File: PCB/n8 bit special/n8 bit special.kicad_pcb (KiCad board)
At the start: 2 copper layers, 99.7 x 97.8 mm, 36 parts, among them J1 PowerPort, J2 PORT0, J3 PORT2, J4 PORT1, J5 PORT3, J6 Conn_02x08_Odd_Even, SW1 SW_Push_Dual, U1 W65C02SxP, U2 CY62256-70PC, U3 CY62256-70PC, U4 28C256, U5 74LS21, U6 22V10C, U7 DS1813, X1 2Mhz

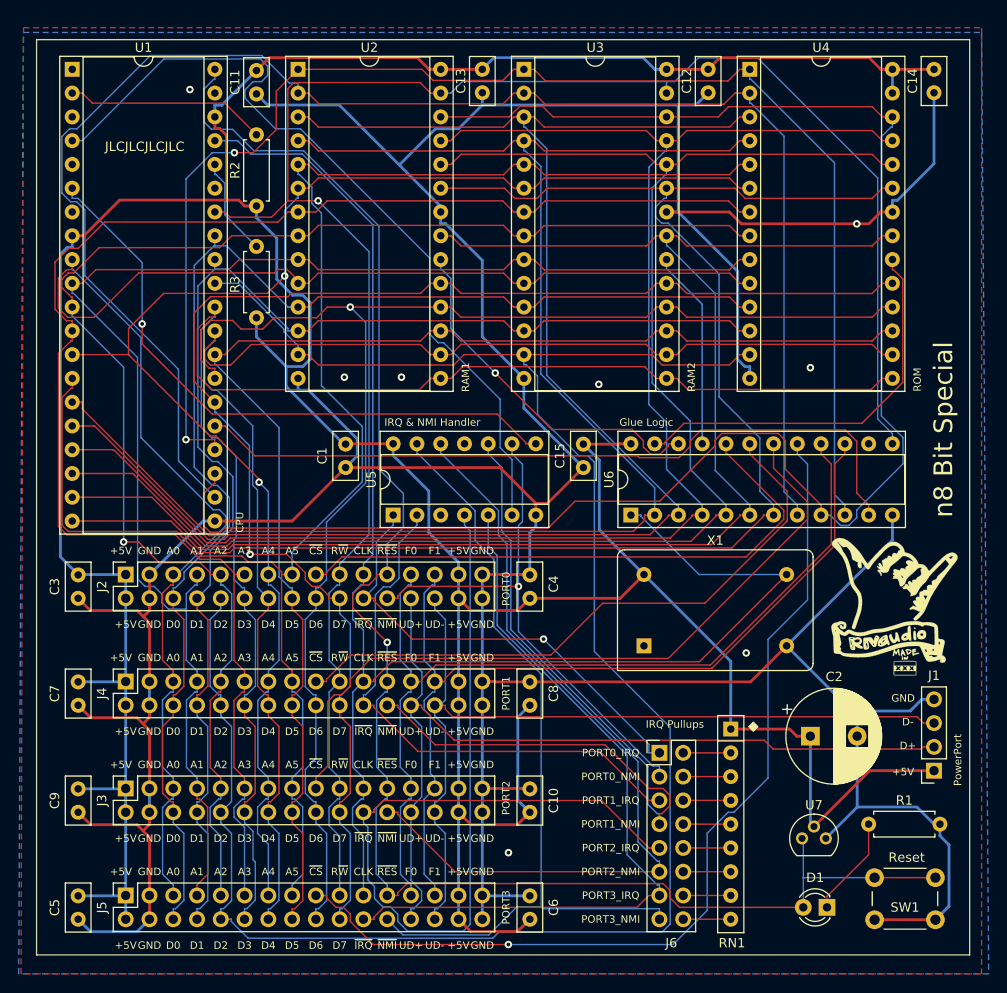
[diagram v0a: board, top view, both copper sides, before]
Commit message: New placement and parts for v2
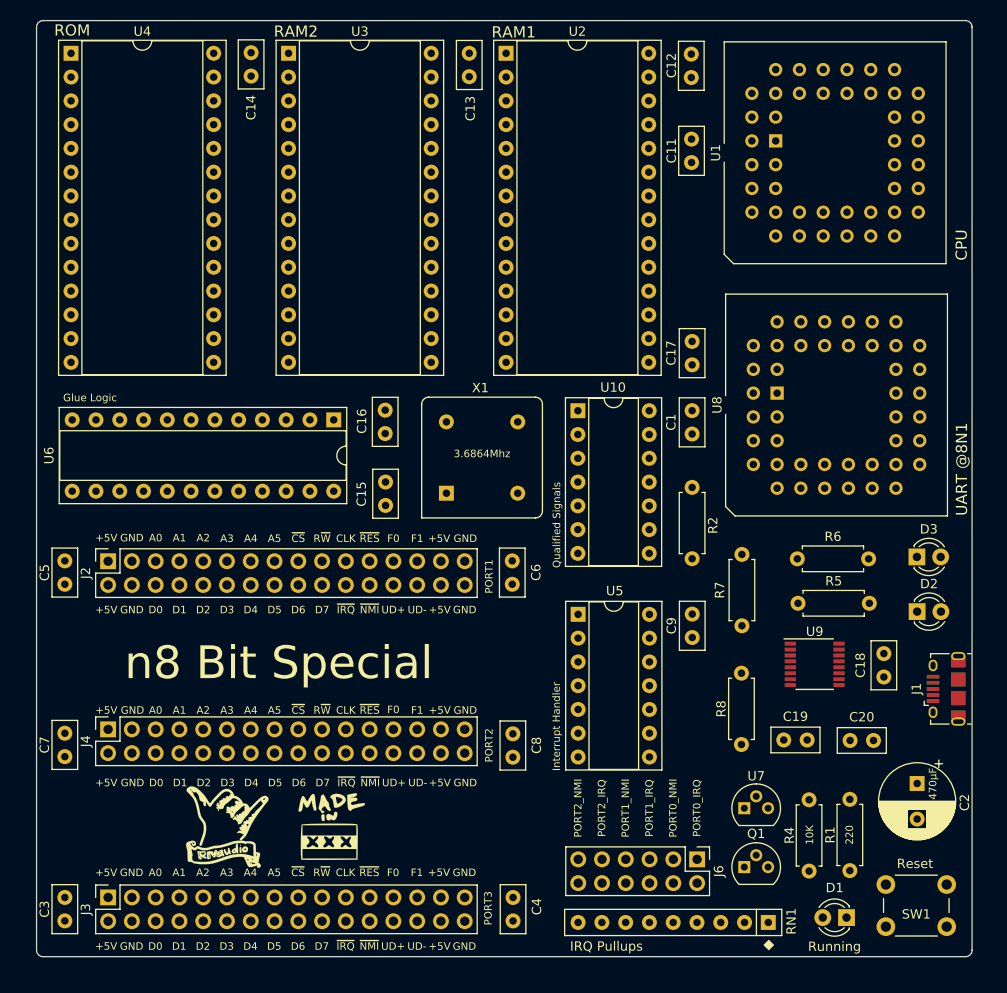
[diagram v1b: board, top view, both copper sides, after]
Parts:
- removed C10: 100nf, Capacitor_THT:C_Disc_D5.0mm_W2.5mm_P2.50mm
- removed J5: PORT3, Connector_PinSocket_2.54mm:PinSocket_2x16_P2.54mm_Vertical
- removed R3: 3K3, Resistor_THT:R_Axial_DIN0207_L6.3mm_D2.5mm_P7.62mm_Horizontal
- added C16: 100nf, Capacitor_THT:C_Disc_D5.0mm_W2.5mm_P2.50mm, F.Cu at (124.2, 84.0)
- added C17: 100nF, Capacitor_THT:C_Disc_D5.0mm_W2.5mm_P2.50mm, F.Cu at (157.0, 76.7)
- added C18: 100nF, Capacitor_THT:C_Disc_D5.0mm_W2.5mm_P2.50mm, F.Cu at (177.5, 110.0)
- added C19: 47pF, Capacitor_THT:C_Disc_D5.0mm_W2.5mm_P2.50mm, F.Cu at (166.8, 116.7)
- added C20: 47pF, Capacitor_THT:C_Disc_D5.0mm_W2.5mm_P2.50mm, F.Cu at (173.9, 116.8)
- added D2: TX, LED_THT:LED_D3.0mm, F.Cu at (181.1, 103.0)
- added D3: RX, LED_THT:LED_D3.0mm, F.Cu at (181.1, 97.2)
- added G***: LOGO, graphics:MadeInAMS, F.Cu at (118.5, 125.8)
- added Q1: 2N3904, Package_TO_SOT_THT:TO-92, F.Cu at (162.6, 130.3)
- added R4: 10K, Resistor_THT:R_Axial_DIN0207_L6.3mm_D2.5mm_P7.62mm_Horizontal, F.Cu at (169.5, 130.7)
- added R5: 220, Resistor_THT:R_Axial_DIN0207_L6.3mm_D2.5mm_P7.62mm_Horizontal, F.Cu at (168.4, 102.1)
- added R6: 220, Resistor_THT:R_Axial_DIN0207_L6.3mm_D2.5mm_P7.62mm_Horizontal, F.Cu at (168.3, 97.4)
- added R7: 27, Resistor_THT:R_Axial_DIN0207_L6.3mm_D2.5mm_P7.62mm_Horizontal, F.Cu at (162.4, 96.9)
- added R8: 27, Resistor_THT:R_Axial_DIN0207_L6.3mm_D2.5mm_P7.62mm_Horizontal, F.Cu at (162.3, 109.6)
- added U10: 74HC00, Package_DIP:DIP-14_W7.62mm_Socket, F.Cu at (144.8, 81.6)
- added U8: SC28L92_PLC44, Package_LCC:PLCC-44_THT-Socket, F.Cu at (166.1, 79.7)
- added U9: FT230XS, Package_SO:SSOP-16_3.9x4.9mm_P0.635mm, F.Cu at (170.1, 108.7)
- C2: value 1000uF -> 470uF; footprint Capacitor_THT:CP_Radial_D10.0mm_P5.00mm -> Capacitor_THT:CP_Radial_D8.0mm_P3.80mm
- C9: value 100nf -> 100nF
- J1: value PowerPort -> USB_B_Micro; footprint Connector_PinSocket_2.54mm:PinSocket_1x04_P2.54mm_Vertical -> Connector_USB:USB_Micro-B_Amphenol_10118194_Horizontal
- J6: footprint Connector_PinHeader_2.54mm:PinHeader_2x08_P2.54mm_Vertical -> Connector_PinHeader_2.54mm:PinHeader_2x06_P2.54mm_Vertical
- R1: value 330 -> 220
- U1: footprint Package_DIP:DIP-40_W15.24mm_Socket -> Package_LCC:PLCC-44_THT-Socket
- X1: value 2Mhz -> 3.6864Mhz; footprint Oscillator:Oscillator_DIP-14 -> Oscillator:Oscillator_DIP-8
- moved U1 75.5 mm to (166.0, 52.7), turned to 90 degrees
- moved G*** 75.2 mm to (107.3, 126.0)
- moved C14 73.0 mm to (109.9, 43.3)
- moved U4 72.5 mm to (90.7, 43.4)
- moved C9 68.9 mm to (157.0, 103.3), turned to 270 degrees
- moved R2 59.9 mm to (157.0, 89.8)
- moved C11 47.5 mm to (157.0, 55.0), turned to 90 degrees
- moved C1 37.2 mm to (157.0, 84.0)
- moved C6 35.8 mm to (137.8, 100.1)
- moved C5 35.8 mm to (90.0, 100.1)
- moved C4 34.5 mm to (137.9, 136.1)
- moved C3 34.5 mm to (90.0, 136.1)
- moved U6 33.3 mm to (118.7, 82.5), turned to 270 degrees
- moved X1 26.7 mm to (130.8, 90.4)
- moved U3 25.2 mm to (113.9, 43.4)
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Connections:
- C9 pad 1: GND -> +5V
- C9 pad 2: +5V -> GND
- D1 pad 2: ~RES -> Net-(D1-Pad2)
- J1 pad 2: USB_D+ -> USB_D-
- J1 pad 3: USB_D- -> USB_D+
- J1 pad 4: GND -> Net-(J1-Pad4)
- J2 pad 26: USB_D+ -> ~READ
- J2 pad 28: USB_D- -> ~WRITE
- J3 pad 26: USB_D+ -> ~READ
- J3 pad 28: USB_D- -> ~WRITE
- J4 pad 26: USB_D+ -> ~READ
- J4 pad 28: USB_D- -> ~WRITE
- R2 pad 1: Net-(R2-Pad1) -> ~UART_IRQ
- RN1 pad 2: Net-(J6-Pad2) -> RDY_PULLUP
- RN1 pad 3: Net-(J6-Pad4) -> BE_PULLUP
- RN1 pad 4: Net-(J6-Pad6) -> Net-(J6-Pad2)
- RN1 pad 5: Net-(J6-Pad8) -> Net-(J6-Pad4)
- RN1 pad 6: Net-(J6-Pad10) -> Net-(J6-Pad6)
- RN1 pad 7: Net-(J6-Pad12) -> Net-(J6-Pad8)
- RN1 pad 8: Net-(J6-Pad14) -> Net-(J6-Pad10)
- RN1 pad 9: Net-(J6-Pad16) -> Net-(J6-Pad12)
- U1 pad 1: Net-(U1-Pad1) -> GND
- U1 pad 10: /A1 -> /A0
- U1 pad 11: /A2 -> /A1
- U1 pad 12: /A3 -> Net-(U1-Pad12)
- U1 pad 13: /A4 -> /A2
- U1 pad 14: /A5 -> /A3
- U1 pad 15: /A6 -> /A4
- U1 pad 16: /A7 -> /A5
- U1 pad 17: /A8 -> /A6
- U1 pad 18: /A9 -> /A7
- U1 pad 19: /A10 -> /A8
- U1 pad 2: Net-(R2-Pad1) -> Net-(U1-Pad2)
- U1 pad 20: /A11 -> /A9
- U1 pad 21: GND -> /A10
- U1 pad 22: /A12 -> /A11
- U1 pad 23: /A13 -> GND
- U1 pad 24: /A14 -> GND
- U1 pad 25: /A15 -> /A12
- U1 pad 26: /D7 -> /A13
- U1 pad 27: /D6 -> /A14
- U1 pad 28: /D5 -> /A15
- U1 pad 29: /D4 -> /D7
- U1 pad 3: Net-(U1-Pad3) -> RDY_PULLUP
- U1 pad 30: /D3 -> /D6
- U1 pad 31: /D2 -> /D5
- U1 pad 32: /D1 -> /D4
- U1 pad 33: /D0 -> /D3
- U1 pad 34: R~W -> /D2
- U1 pad 35: Net-(U1-Pad35) -> /D1
- U1 pad 36: Net-(R3-Pad1) -> /D0
- U1 pad 37: CLK -> +5V
- U1 pad 38: +5V -> R~W
- U1 pad 4: ~IRQ -> Net-(U1-Pad4)
- U1 pad 40: ~RES -> BE_PULLUP
- U1 pad 5: Net-(U1-Pad5) -> ~IRQ
- U1 pad 6: ~NMI -> Net-(U1-Pad6)
- U1 pad 7: Net-(U1-Pad7) -> ~NMI
- U1 pad 8: +5V -> Net-(U1-Pad8)
- U1 pad 9: /A0 -> +5V
- U2 pad 22: GND -> ~READ
- U2 pad 27: R~W -> ~WRITE
- U3 pad 22: GND -> ~READ
- U3 pad 27: R~W -> ~WRITE
- U4 pad 22: GND -> ~READ
- U5 pad 13: PORT3_NMI_PULLUP -> +5V
- U5 pad 5: PORT3_IRQ_PULLUP -> ~UART_IRQ
- U6 pad 14: Net-(U6-Pad14) -> FUTURE1
- U6 pad 15: FUTURE1 -> FUTURE0
- U6 pad 16: FUTURE0 -> Net-(U6-Pad16)
- U6 pad 17: ~PORT3_CS -> ~UART_CS
- X1 pad 8: CLK -> +5V
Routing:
- net GND: track 483.3 -> 0.00 mm, vias 8 -> 0
- net +5V: track 438.1 -> 0.00 mm
- net /D2: track 218.0 -> 0.00 mm
- net R~W: track 205.8 -> 0.00 mm, vias 1 -> 0
- net /A13: track 184.3 -> 0.00 mm
- net /A5: track 180.0 -> 0.00 mm
- net ~RES: track 177.3 -> 0.00 mm, vias 1 -> 0
- net /A12: track 174.3 -> 0.00 mm
- net /A7: track 170.6 -> 0.00 mm
- net /A11: track 169.3 -> 0.00 mm
- net /A3: track 167.5 -> 0.00 mm
- net /A0: track 166.3 -> 0.00 mm
- net /A9: track 166.0 -> 0.00 mm
- net /A8: track 166.0 -> 0.00 mm
- net /A6: track 165.7 -> 0.00 mm
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- removed copper zone on B.Cu, net GND
- removed copper zone on F.Cu, net GND
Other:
- board size 99.7 x 97.8 mm -> 99.9 x 100 mm
- net class Power: clearance 0.3 -> 0.2
- board text added: "10K"
- board text added: "220"
- board text added: "3.6864Mhz"
- board text added: "470µF"
- board text added: "Interrupt Handler"
- board text added: "Qualified Signals"
- board text added: "Running"
- board text added: "UART @8N1"
- board text added: "by Nate Rivard https://github.com/nrivard/lmaos Version 2 Mar 2021"
- board text removed: "D+"
- board text removed: "D-"
- board text removed: "IRQ & NMI Handler"
- board text removed: "JLCJLCJLCJLC"
- board text removed: "PORT0"
- board text removed: "PORT3_IRQ"
- board text removed: "PORT3_NMI"
- board text removed: "PowerPort"
- board text removed: "by Nate Rivard https://github.com/nrivard/lmaos Version 1 Mar 2021"

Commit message: Used Freerouter to route 4 layer PCB
Had to touch up inner well area on the UART as it was disconnected to the rest of the power plane.
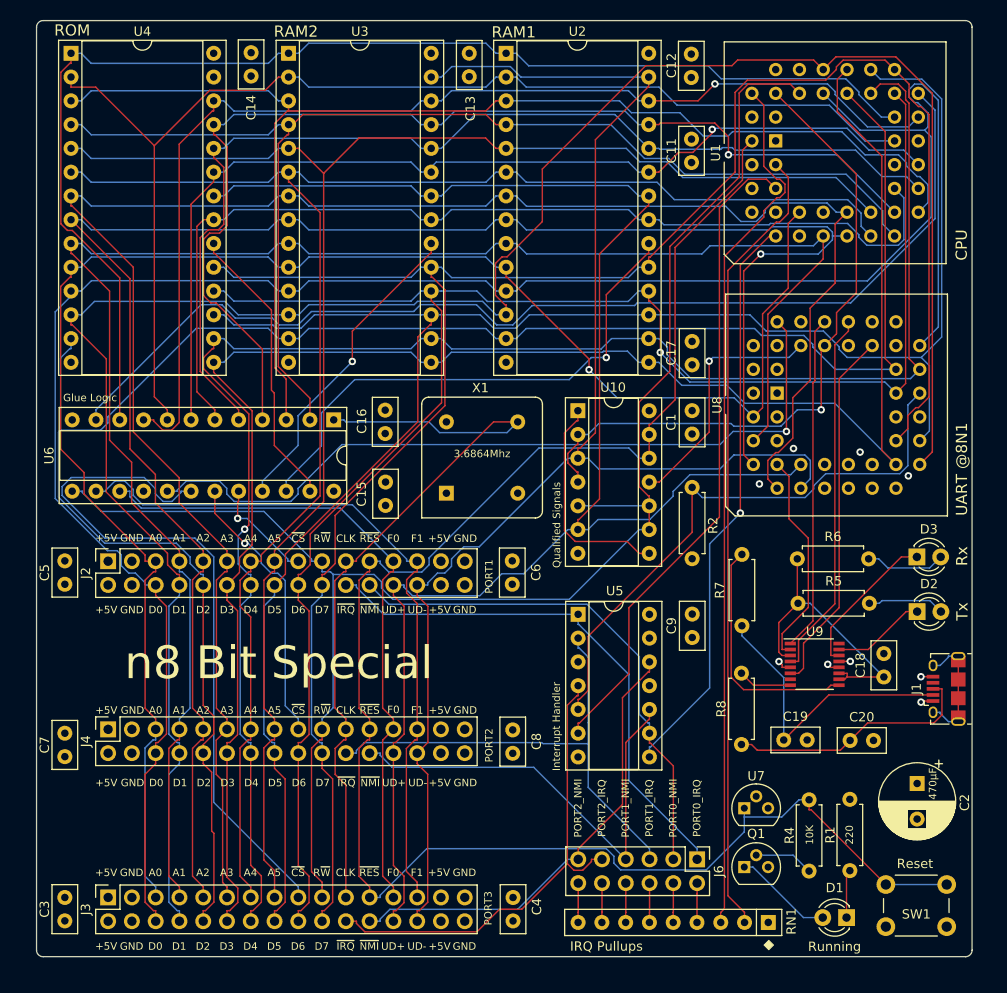
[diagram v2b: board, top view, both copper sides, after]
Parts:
- removed G***: LOGO, graphics:MadeInAMS
- removed G***: LOGO, graphics:Shaka
- moved C8 0.42 mm to (137.9, 118.2)
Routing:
- net /D0: track 0.00 -> 232.2 mm
- net /D1: track 0.00 -> 228.6 mm
- net /D7: track 0.00 -> 211.2 mm
- net /D2: track 0.00 -> 205.5 mm
- net /A3: track 0.00 -> 204.7 mm
- net /D5: track 0.00 -> 201.1 mm
- net /A2: track 0.00 -> 198.8 mm, vias 0 -> 1
- net /D6: track 0.00 -> 191.9 mm, vias 0 -> 1
- net /D3: track 0.00 -> 189.3 mm
- net ~RES: track 0.00 -> 188.1 mm
- net /A1: track 0.00 -> 185.3 mm
- net /D4: track 0.00 -> 182.8 mm, vias 0 -> 1
- net /A0: track 0.00 -> 181.5 mm, vias 0 -> 1
- net /A4: track 0.00 -> 175.8 mm
- net ~READ: track 0.00 -> 175.6 mm
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- added copper zone on PWR_PLANE, net +5V
- added copper zone on GND_PLANE, net GND
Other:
- copper layers 2 -> 4
- board text added: "Rx"
- board text added: "Tx"

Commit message: Layout centered around USB D+/D- differential pair
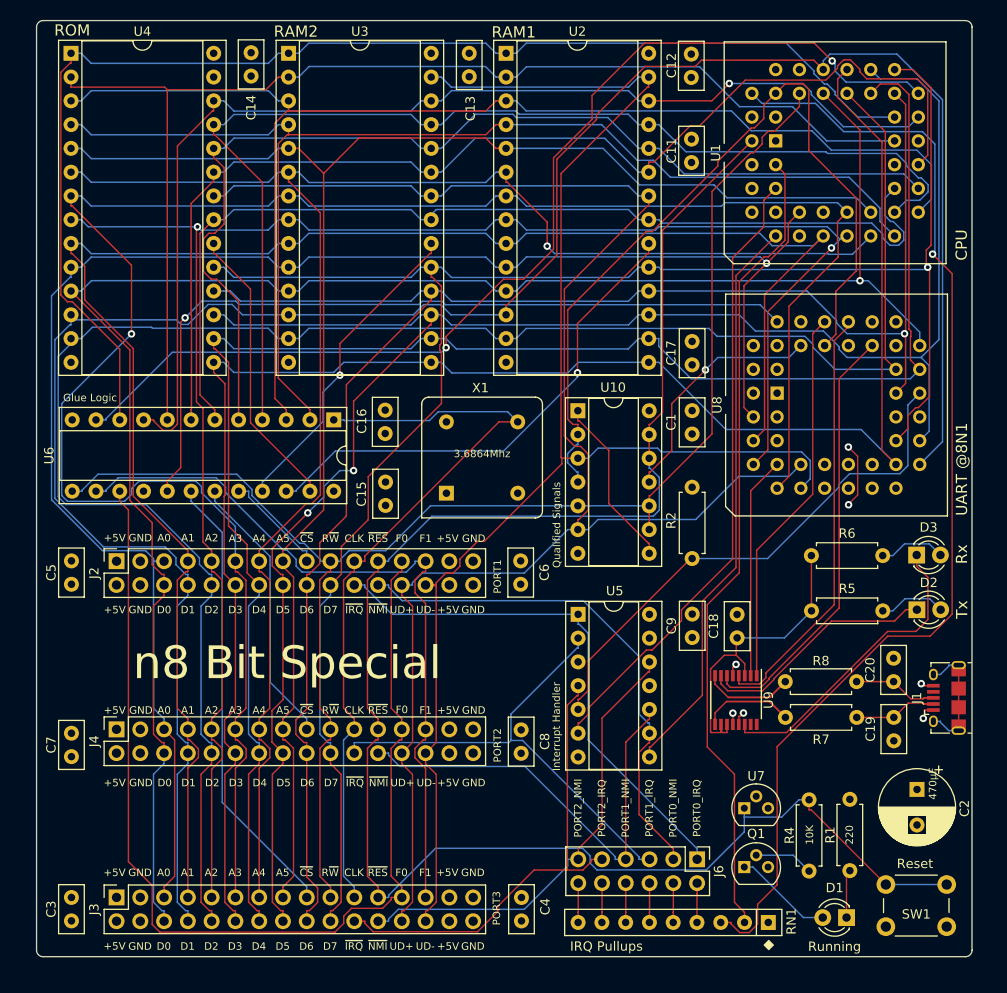
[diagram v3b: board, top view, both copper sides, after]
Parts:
- moved R7 18.0 mm to (167.0, 114.3), turned to 0 degrees
- moved C18 16.2 mm to (161.8, 105.8)
- moved C19 12.0 mm to (178.6, 114.3), turned to 270 degrees
- moved U9 9.24 mm to (161.7, 112.5), turned to 270 degrees
- moved C20 7.82 mm to (178.6, 110.5), turned to 90 degrees
- moved R2 7.60 mm to (157.0, 97.4), turned to 90 degrees
- moved R8 4.77 mm to (167.0, 110.5), turned to 0 degrees
- moved R5 1.65 mm to (169.8, 102.9)
- moved R6 1.54 mm to (169.8, 97.0)
- moved J1 0.97 mm to (184.2, 112.2)
- moved J2 0.90 mm to (95.5, 97.6)
- moved J3 0.90 mm to (95.5, 133.6)
- moved J4 0.90 mm to (95.5, 115.6)
- moved C4 0.90 mm to (138.8, 136.1)
- moved C6 0.90 mm to (138.7, 100.1)
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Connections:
- net Net-(R7-Pad1) renamed /F_USB_D-
- net Net-(R8-Pad1) renamed /F_USB_D+
- U9 pad 15: Net-(D2-Pad1) -> Net-(U9-Pad15)
- U9 pad 7: Net-(U9-Pad7) -> Net-(D2-Pad1)
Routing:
- net FUTURE0: track 70.7 -> 114.9 mm
- net /D0: track 232.2 -> 192.0 mm, vias 0 -> 1
- net BE_PULLUP: track 93.3 -> 122.2 mm, vias 0 -> 1
- net ~PORT2_CS: track 76.1 -> 48.5 mm
- net USB_D-: track 32.0 -> 8.86 mm
- net USB_D+: track 27.0 -> 9.00 mm
- net Net-(D3-Pad1): track 16.2 -> 32.8 mm
- net Net-(D2-Pad1): track 10.0 -> 25.7 mm
- net /A3: track 204.7 -> 220.4 mm, vias 0 -> 1
- net /F_USB_D-: track 25.9 -> 10.6 mm
- net CLK: track 162.9 -> 177.6 mm, vias 1 -> 0
- net /A11: track 108.9 -> 123.5 mm, vias 1 -> 0
- net R~W: track 173.3 -> 161.5 mm
- net /D7: track 211.2 -> 200.3 mm, vias 0 -> 1
- net /A2: track 198.8 -> 188.5 mm, vias 1 -> 2
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
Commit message: v2 release candidate
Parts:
- added G***: LOGO, graphics:MadeInAMS, F.Cu at (119.3, 125.7)
- added G***: LOGO, graphics:Shaka, F.Cu at (110.5, 125.8)
- moved R2 23.2 mm to (138.7, 111.7)
- moved C2 0.39 mm to (181.4, 122.3)
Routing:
- net /D4: track 181.3 -> 243.9 mm
- net FUTURE0: track 114.9 -> 77.6 mm, vias 0 -> 1
- net /D6: track 186.0 -> 221.7 mm, vias 1 -> 0
- net CLK: track 177.6 -> 151.3 mm
- net /A3: track 220.4 -> 198.7 mm, vias 1 -> 0
- net PORT0_NMI_PULLUP: track 55.5 -> 75.9 mm
- net /D3: track 187.2 -> 207.0 mm
- net /D1: track 235.0 -> 216.3 mm
- net /D0: track 192.0 -> 210.3 mm, vias 1 -> 0
- net /A15: track 115.2 -> 133.4 mm, vias 2 -> 0
- net PORT1_IRQ_PULLUP: track 52.2 -> 66.0 mm
- net /D5: track 201.4 -> 215.1 mm, vias 2 -> 1
- net /A11: track 123.5 -> 110.6 mm
- net /D2: track 201.3 -> 213.0 mm
- net ~UART_CS: track 84.5 -> 73.0 mm, vias 1 -> 0
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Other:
- board text added: "JLCJLCJLCJLC"
- board text added: "by Nate Rivard https://github.com/nrivard/n8-bit Version 2 Sept 2021"
- board text added: "~RD"
- board text added: "~WR"
- board text removed: "UD+"
- board text removed: "UD-"
- board text removed: "by Nate Rivard https://github.com/nrivard/lmaos Version 2 Mar 2021"
